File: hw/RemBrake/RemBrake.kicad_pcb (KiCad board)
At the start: 2 copper layers, 40 x 80 mm, 110 parts, among them IC1 LTC2943IDD#TRPBF, J1 Screw_Terminal_01x02, J2 Conn_01x03_MountingPin, J3 Screw_Terminal_01x04, J4 Conn_01x08_MountingPin, J5 Conn_01x04_MountingPin, J6 Conn_01x03_MountingPin, J7 Conn_01x07, J8 Conn_01x07, J9 Conn_01x03, Q1 SiS415DNT, Q2 BC337, Q3 BC847, Q4 BC337, Q5 BC847, Q6 BC337, Q7 BC847, Q8 BC337, Q9 BC847, U1 TPS62140, U2 BD48ExxG, U3 XC6220B331MR, U4 MAX40200AUK, U5 LM555xN, U6 MAX40200AUK, U7 MAX40200AUK

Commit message: added 555 counter output divider to adjust to 3v3 voltage level
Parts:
- added R46: 5k, Resistor_SMD:R_0805_2012Metric_Pad1.20x1.40mm_HandSolder, B.Cu at (127.6, 104.1)
- added R47: 5k, Resistor_SMD:R_0805_2012Metric_Pad1.20x1.40mm_HandSolder, B.Cu at (128.9, 106.6)
- added REF**: OSHW-Symbol_6.7x6mm_SilkScreen, Symbol:OSHW-Symbol_6.7x6mm_SilkScreen, B.Cu at (153.4, 66.6)
- added REF**: WEEE-Logo_4.2x6mm_SilkScreen, Symbol:WEEE-Logo_4.2x6mm_SilkScreen, B.Cu at (153.4, 74.1)
- renumbered R46 to R48, R47 to R49, R48 to R50, R49 to R51, R50 to R52, R51 to R53, R52 to R54, R53 to R55, R54 to R56, R55 to R57, R56 to R58, R57 to R59, R58 to R60, R59 to R61, R60 to R62, R61 to R63
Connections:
- U5 pad 3: Net-(D3-A) -> Net-(U5-Q)
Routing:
- added copper zone on B.Cu, net Net-(U5-Q)

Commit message: updated pcb and added todo in the schematic
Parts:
- added D3: MBR0520, Diode_SMD:D_SOD-123, F.Cu at (135.6, 123.7)
- added R46: 536k, Resistor_SMD:R_0805_2012Metric_Pad1.20x1.40mm_HandSolder, F.Cu at (131.9, 124.5)
- C5, C6: value 220nF -> 0.1uF
- R17, R3, R33, R39: value 5k -> 5k1
- R28, R29, R30: value 100R -> 110R
- R36: value 200R -> 110R
- R47: renamed from R46; value 5k -> 5k1
- R48: renamed from R47; value 5k -> 10k
- R49: renamed from R48; value 5k -> 2k7
- R55: renamed from R54; value 5k -> 5k1
- R59: renamed from R58; value 590k -> 10k
- R9: value 590k -> 536k
- moved C10 3.74 mm to (137.3, 129.1), turned to -90 degrees
- moved C7 3.11 mm to (132.2, 121.5), turned to 0 degrees
- moved R59 2.54 mm to (136.3, 126.0)
- moved C9 1.89 mm to (135.0, 129.1), turned to -90 degrees
- moved C8 0.54 mm to (132.7, 129.1), turned to -90 degrees
- moved R30 0.16 mm to (136.3, 121.5)
- renumbered D3 to D4, R49 to R50, R50 to R51, R51 to R52, R52 to R53, R53 to R54, R55 to R56, R56 to R57, R57 to R58, R59 to R60, R60 to R61, R61 to R62, R62 to R63, R63 to R64
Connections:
- C7 pad 1: /brake_control/STATUS -> Net-(D3-A)
- U5 pad 4: /brake_control/STATUS -> Net-(D3-A)
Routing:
- net Net-(D3-A): track 0.00 -> 23.5 mm
- net /brake_control/STATUS: track 67.3 -> 59.1 mm
- net /brake_control/ENABLE: track 55.3 -> 58.1 mm
- net /brake_control/BUZZER: track 33.1 -> 35.6 mm
- net +5V: track 76.8 -> 78.9 mm
- net /brake_control/I2C.SDA: track 92.9 -> 94.5 mm
- net +3V3: track 108.4 -> 107.0 mm
- net /brake_control/I2C.SCL: track 85.6 -> 87.0 mm
- net GND: vias 6 -> 7
- added copper zone on F.Cu, net Net-(D3-A)

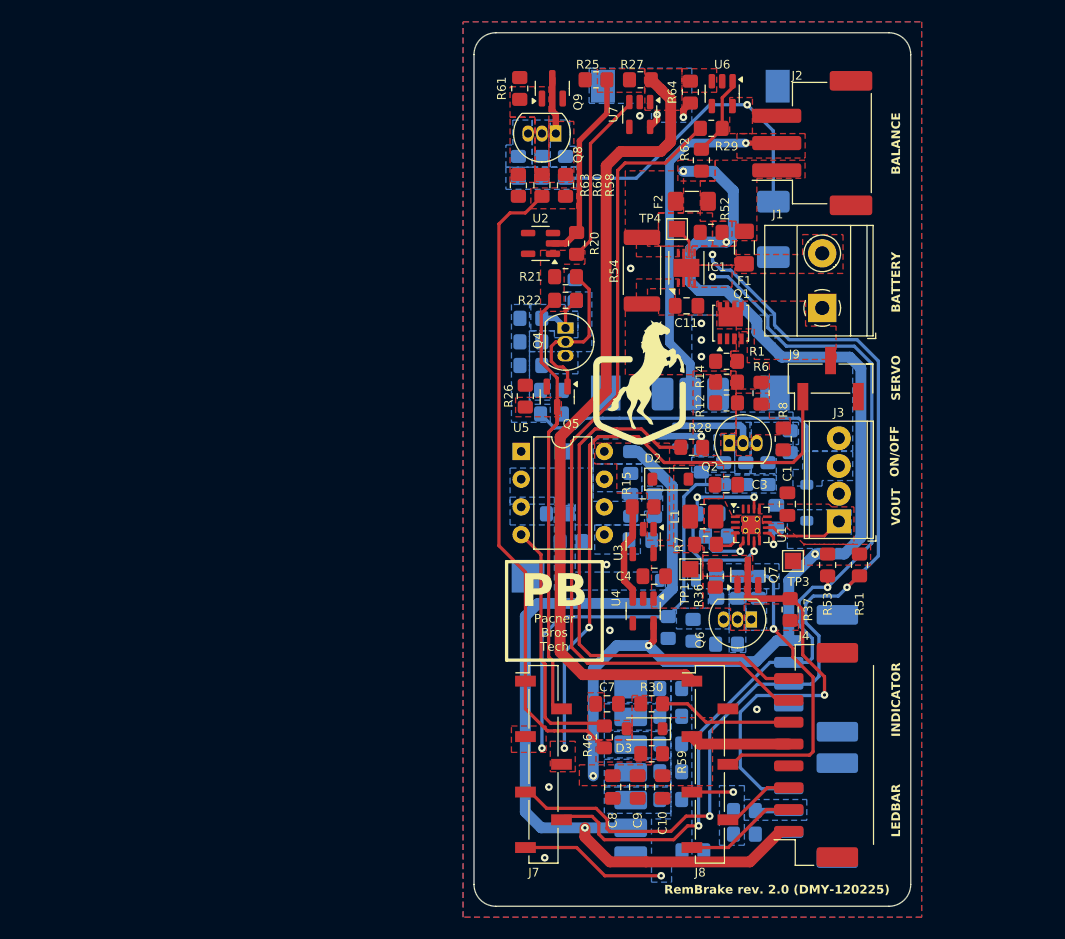
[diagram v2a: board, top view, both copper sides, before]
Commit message: replaced optocoupler with transistor and loaded components in the pcb sheet
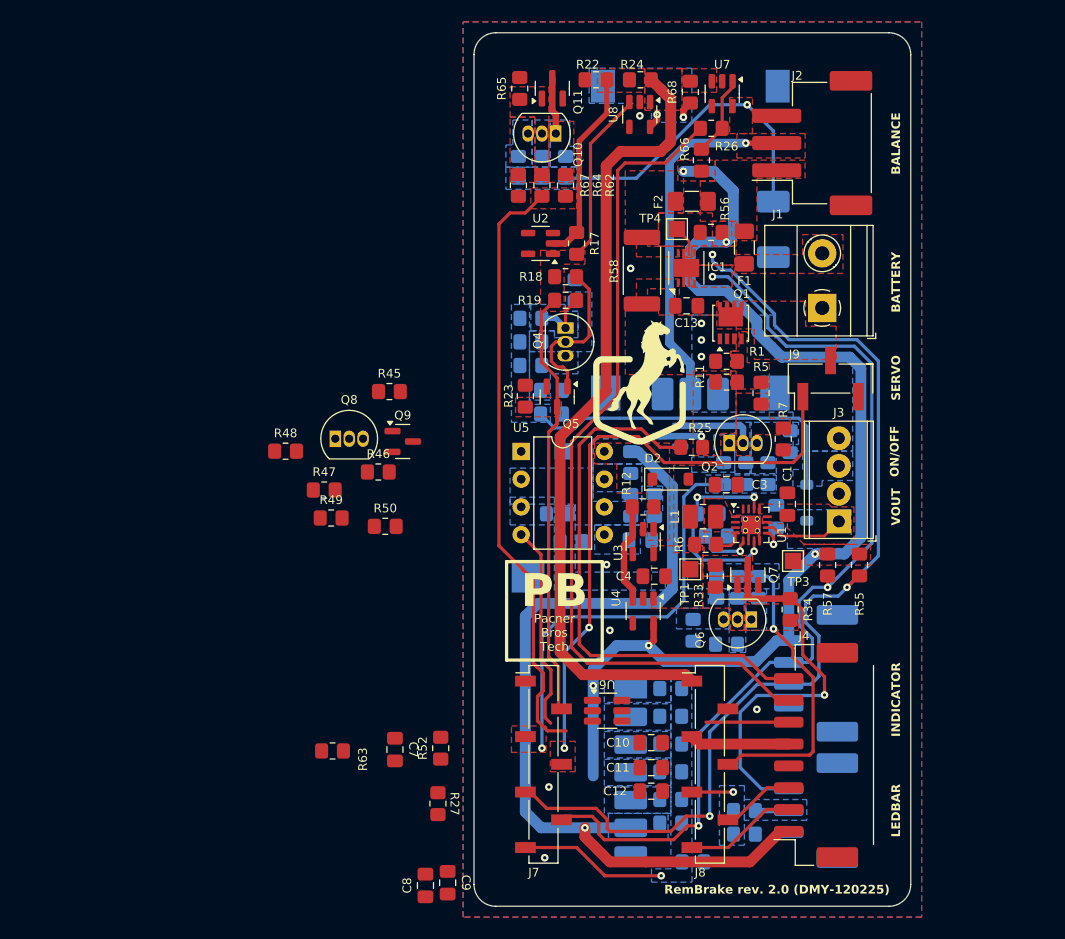
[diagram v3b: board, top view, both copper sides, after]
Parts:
- removed D3, D4: MBR0520, Diode_SMD:D_SOD-123
- removed the R11 at (140.8, 99.2)
- removed the R12 at (143.1, 93.9)
- removed the R2 at (137.8, 114.5)
- removed REF**: OSHW-Symbol_6.7x6mm_SilkScreen, Symbol:OSHW-Symbol_6.7x6mm_SilkScreen
- removed REF**: WEEE-Logo_4.2x6mm_SilkScreen, Symbol:WEEE-Logo_4.2x6mm_SilkScreen
- added C8: 0.33uF, Capacitor_SMD:C_0805_2012Metric_Pad1.18x1.45mm_HandSolder, F.Cu at (115.6, 138.1)
- added C9: 0.33uF, Capacitor_SMD:C_0805_2012Metric_Pad1.18x1.45mm_HandSolder, F.Cu at (117.6, 137.8)
- added Q8: BC337, Package_TO_SOT_THT:TO-92_Inline, F.Cu at (107.3, 97.2)
- added Q9: BC847, Package_TO_SOT_SMD:SOT-23, F.Cu at (113.5, 97.4)
- added R45: 100k, Resistor_SMD:R_0805_2012Metric_Pad1.20x1.40mm_HandSolder, F.Cu at (112.3, 92.9)
- added R47: 5k, Resistor_SMD:R_0805_2012Metric_Pad1.20x1.40mm_HandSolder, F.Cu at (106.3, 101.9)
- added R48: 5k, Resistor_SMD:R_0805_2012Metric_Pad1.20x1.40mm_HandSolder, F.Cu at (102.7, 98.3)
- added R49: 0R, Resistor_SMD:R_0805_2012Metric_Pad1.20x1.40mm_HandSolder, F.Cu at (106.9, 104.4)
- added R50: 0R, Resistor_SMD:R_0805_2012Metric_Pad1.20x1.40mm_HandSolder, F.Cu at (111.9, 105.2)
- added R51: 100k, Resistor_SMD:R_0805_2012Metric_Pad1.20x1.40mm_HandSolder, B.Cu at (138.0, 132.4)
- added R52: 5k1, Resistor_SMD:R_0805_2012Metric_Pad1.20x1.40mm_HandSolder, F.Cu at (117.0, 125.5)
- added U6: BD5230G-TR, Package_TO_SOT_SMD:SOT-23-6_Handsoldering, F.Cu at (132.2, 122.1)
- C7: value 47uF -> 680pF
- R46: value 536k -> 5k1
- moved R46 31.9 mm to (111.2, 100.2), turned to 0 degrees
- moved R63 29.2 mm to (107.0, 125.8)
- moved R27 21.6 mm to (116.7, 130.6), turned to -90 degrees
- moved C7 19.9 mm to (112.8, 125.6), turned to -90 degrees
- moved C10 5.39 mm to (136.2, 125.0), turned to 180 degrees
- moved C11 2.17 mm to (136.2, 127.3), turned to 180 degrees
- moved C12 1.11 mm to (136.2, 129.5), turned to 180 degrees
- moved R42 1.02 mm to (140.1, 135.9)
- renumbered C8 to C10, C9 to C11, C10 to C12, C11 to C13, Q8 to Q10, Q9 to Q11, R13 to R10, R14 to R11, R15 to R12, R16 to R13, R17 to R14, R18 to R15, R19 to R16, R20 to R17, R21 to R18, R22 to R19, R3 to R2, R23 to R20, R24 to R21, R25 to R22, R26 to R23, R27 to R24, R28 to R25, R29 to R26, R30 to R27, R31 to R28, R32 to R29, R4 to R3, R33 to R30, R34 to R31, R35 to R32, R36 to R33, R37 to R34, R38 to R35, R39 to R36, R40 to R37, R41 to R38, R42 to R39, R5 to R4, R43 to R40, R44 to R41, R45 to R42, R47 to R43, R48 to R44, R6 to R5, R49 to R53, R50 to R54, R51 to R55, R52 to R56, R53 to R57, R54 to R58, R55 to R59, R7 to R6, R56 to R60, R57 to R61, R58 to R62, R59 to R63, R60 to R64, R61 to R65, R62 to R66, R63 to R67, R64 to R68, R8 to R7, R9 to R8, R10 to R9, U6 to U7, U7 to U8
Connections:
- C7 pad 1: Net-(D3-A) -> /brake_control/STATUS
- J7 pad 1: /brake_control/STATUS -> /brake_control/READY
- J7 pad 3: /brake_control/POWER SW -> /brake_control/POWER
- Q3 pad 3: /control_connector/LED RED -> Net-(Q2-C)
- R11 pad 1: /control_connector/LED RED -> Net-(Q2-C)
- R2 pad 1: /brake_control/POWER SW -> /brake_control/POWER
- R25 pad 1: /control_connector/LED RED -> /brake_control/RUNNIG (RED)
- R3 pad 1: /brake_control/POWER SW -> /brake_control/POWER
- R4 pad 1: /brake_control/POWER SW -> /brake_control/POWER
- R43 pad 2: Net-(D4-A) -> /brake_control/BUZZ
- R44 pad 2: Net-(D4-A) -> /brake_control/BUZZ
- R46 pad 1: Net-(D3-A) -> /brake_control/POWER
- R46 pad 2: /brake_control/STATUS -> /brake_control/RUNNIG (RED)
- U5 pad 4: Net-(D3-A) -> /brake_control/BEEP
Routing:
- net /brake_control/POWER SW: track 37.7 -> 0.00 mm, vias 1 -> 0
- net /brake_control/POWER: track 0.00 -> 37.7 mm, vias 0 -> 1
- net Net-(D3-A): track 23.5 -> 0.00 mm
- net /brake_control/BEEP: track 0.00 -> 18.8 mm
- net /control_connector/LED RED: track 5.28 -> 0.00 mm, vias 1 -> 0
- net (no net): track 0.00 -> 5.28 mm
- net /control_connector/BLUE: track 12.4 -> 7.59 mm
- net /brake_control/STATUS: track 59.1 -> 55.9 mm
- net /brake_control/RUNNIG (RED): vias 0 -> 1
- added copper zone on B.Cu, net /brake_control/POWER
- added copper zone on F.Cu, net /brake_control/POWER
- added copper zone on F.Cu, net Net-(Q2-C)
- added copper zone on B.Cu, net Net-(Q8-B)
- added copper zone on F.Cu, net Net-(Q8-B)
- added copper zone on B.Cu, net Net-(Q8-E)
- added copper zone on F.Cu, net Net-(Q8-E)
- removed copper zone on B.Cu, net /brake_control/POWER SW
- removed copper zone on F.Cu, net /brake_control/POWER SW
- removed copper zone on F.Cu, net /control_connector/LED RED
- removed copper zone on F.Cu, net Net-(D3-A)
- removed copper zone on B.Cu, net Net-(D4-A)
- removed copper zone on B.Cu, net Net-(Q10-B)
- removed copper zone on F.Cu, net Net-(Q10-B)
- removed copper zone on B.Cu, net Net-(Q10-E)
- removed copper zone on F.Cu, net Net-(Q10-E)

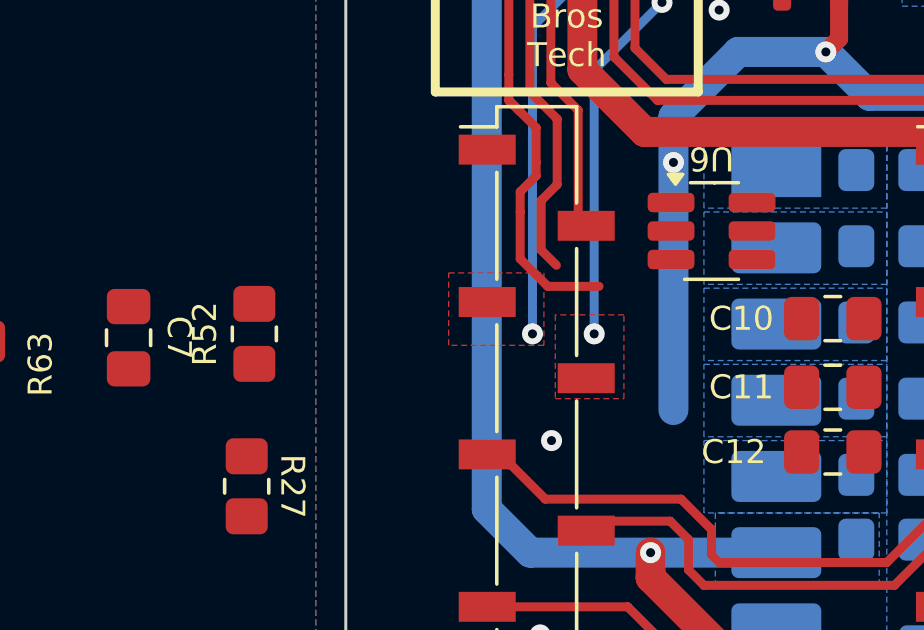
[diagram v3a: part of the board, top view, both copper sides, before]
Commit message: version update and added missing connection between VBUS and 5V
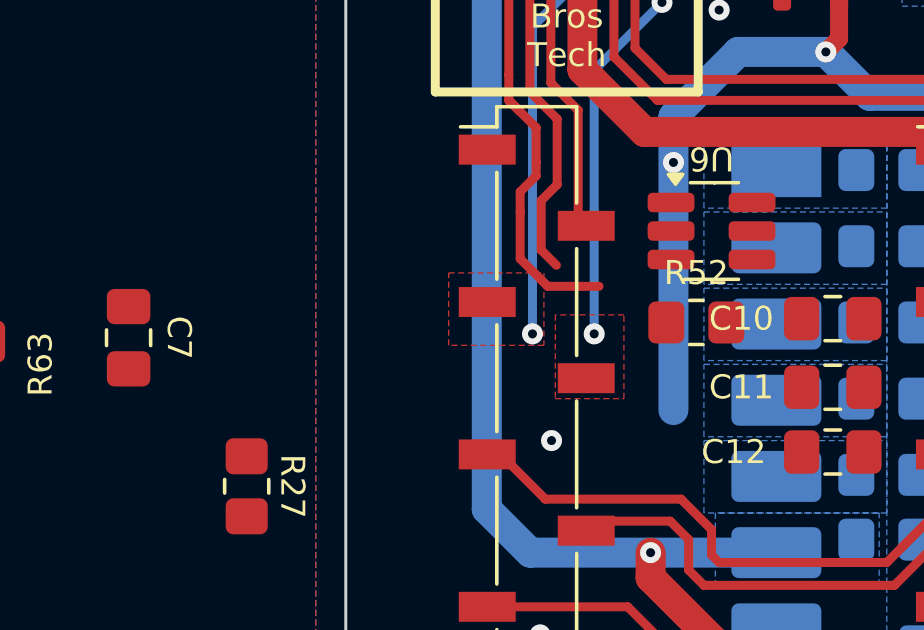
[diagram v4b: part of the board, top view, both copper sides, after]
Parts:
- moved R52 14.7 mm to (131.7, 125.1), turned to 0 degrees

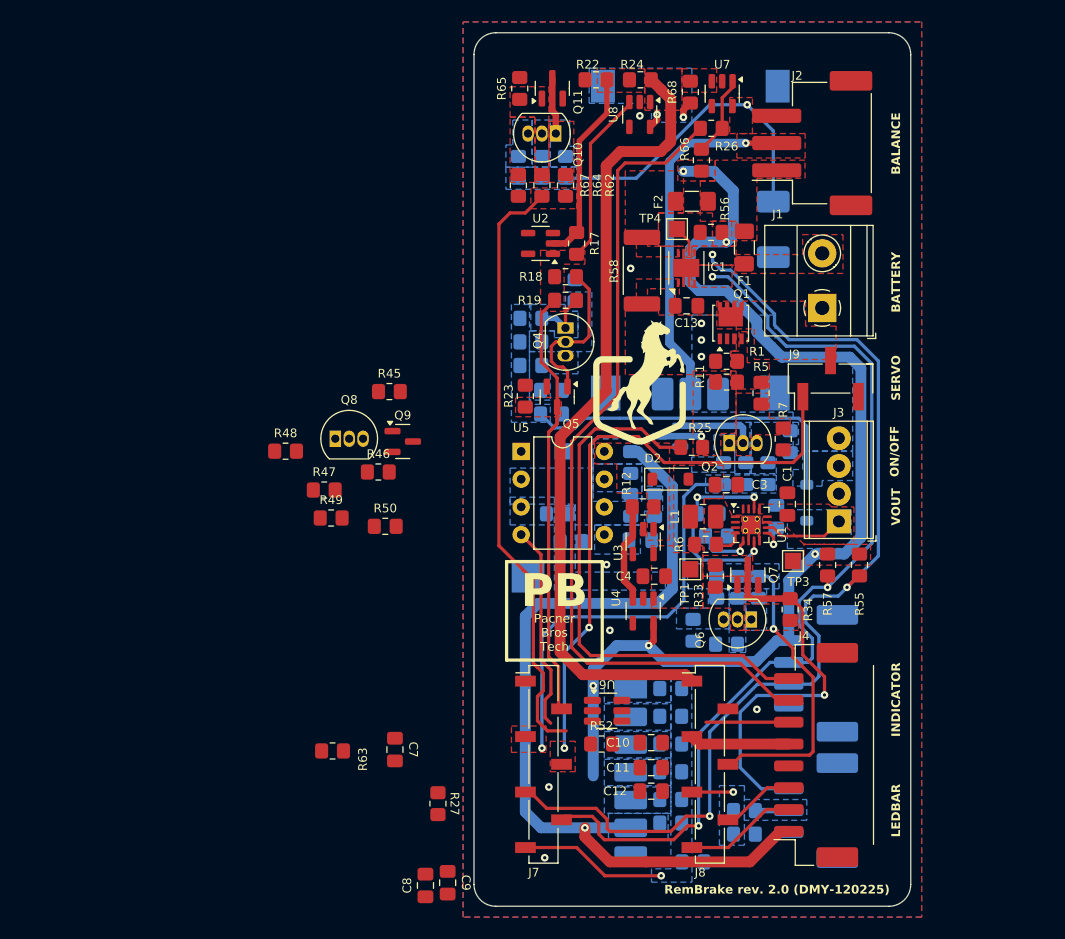
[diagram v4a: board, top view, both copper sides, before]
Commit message: added diodes to connect voltages to display and remote button even when connected to charger
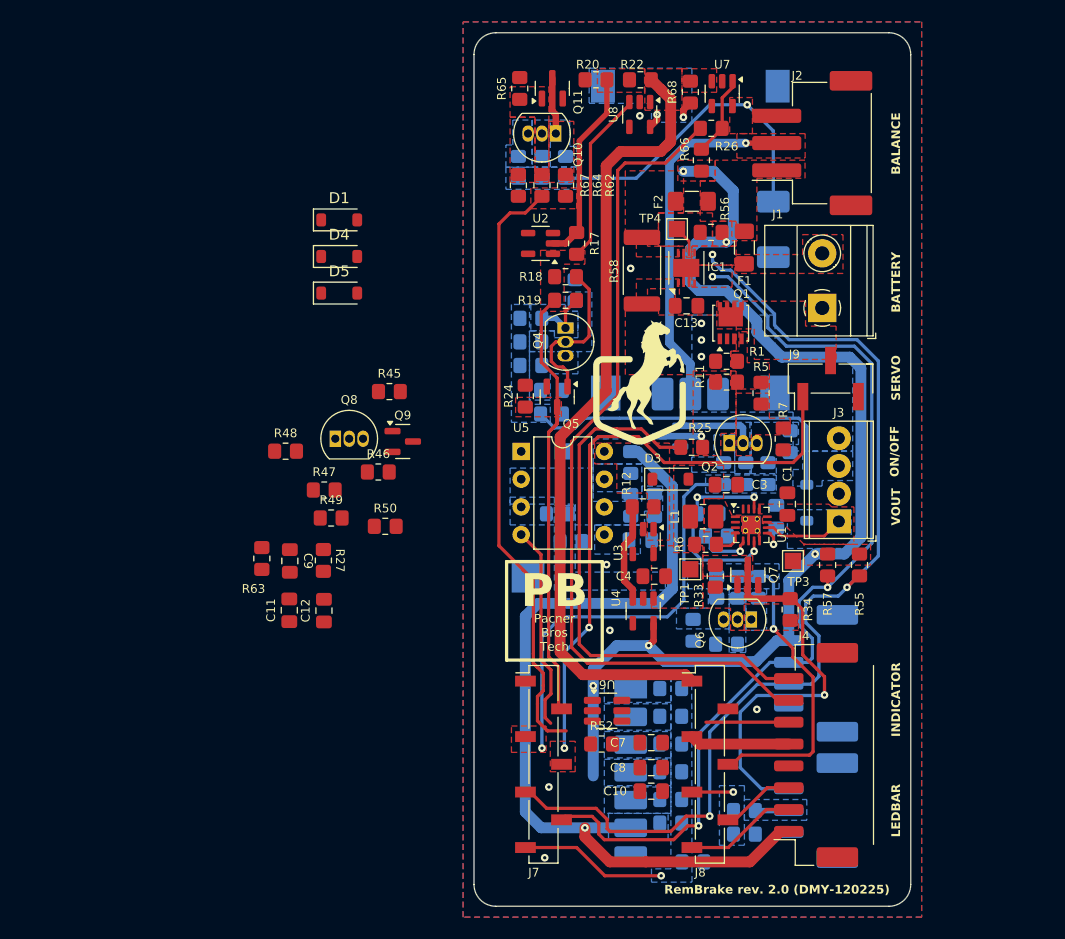
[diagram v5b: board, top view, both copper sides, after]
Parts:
- added D1: MBR0520, Diode_SMD:D_SOD-123, F.Cu at (107.7, 77.1)
- added D4: MBR0520, Diode_SMD:D_SOD-123, F.Cu at (107.7, 80.5)
- added D5: MBR0520, Diode_SMD:D_SOD-123, F.Cu at (107.7, 83.8)
- moved C11 28.1 mm to (103.1, 112.9)
- moved C12 27.4 mm to (106.3, 112.9), turned to 90 degrees
- moved R27 24.6 mm to (106.2, 108.3)
- moved C9 19.8 mm to (103.1, 108.4)
- moved R63 18.8 mm to (100.6, 108.1), turned to 90 degrees
- renumbered C12 to C10, C8 to C11, C9 to C12, C10 to C7, C11 to C8, C7 to C9, D1 to D2, D2 to D3, R22 to R20, R20 to R21, R24 to R22, R21 to R23, R23 to R24
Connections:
- C1 pad 1: /power_switch/BOOST -> Net-(D2-K)
- C3 pad 1: Net-(D2-A) -> +5V
- D2 pad 1: /power_switch/BOOST -> Net-(D2-K)
- D3 pad 1: +5V -> VDD
- D3 pad 2: Net-(D2-A) -> +5V
- J4 pad 1: +5V -> VDD
- L1 pad 2: Net-(D2-A) -> +5V
- M1 pad 6: +5V -> VDD
- R6 pad 1: Net-(D2-A) -> +5V
- R8 pad 1: Net-(D2-A) -> +5V
- U1 pad 10: /power_switch/BOOST -> Net-(D2-K)
- U1 pad 11: /power_switch/BOOST -> Net-(D2-K)
- U1 pad 12: /power_switch/BOOST -> Net-(D2-K)
- U1 pad 13: /power_switch/BOOST -> /power_switch/ON/OFF
- U1 pad 14: Net-(D2-A) -> +5V
- U1 pad 7: Net-(D2-A) -> +5V
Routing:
- net Net-(D2-A): track 23.9 -> 0.00 mm, vias 3 -> 0
- net +5V: track 78.9 -> 102.8 mm, vias 1 -> 4
- removed copper zone on F.Cu, net Net-(D2-A)

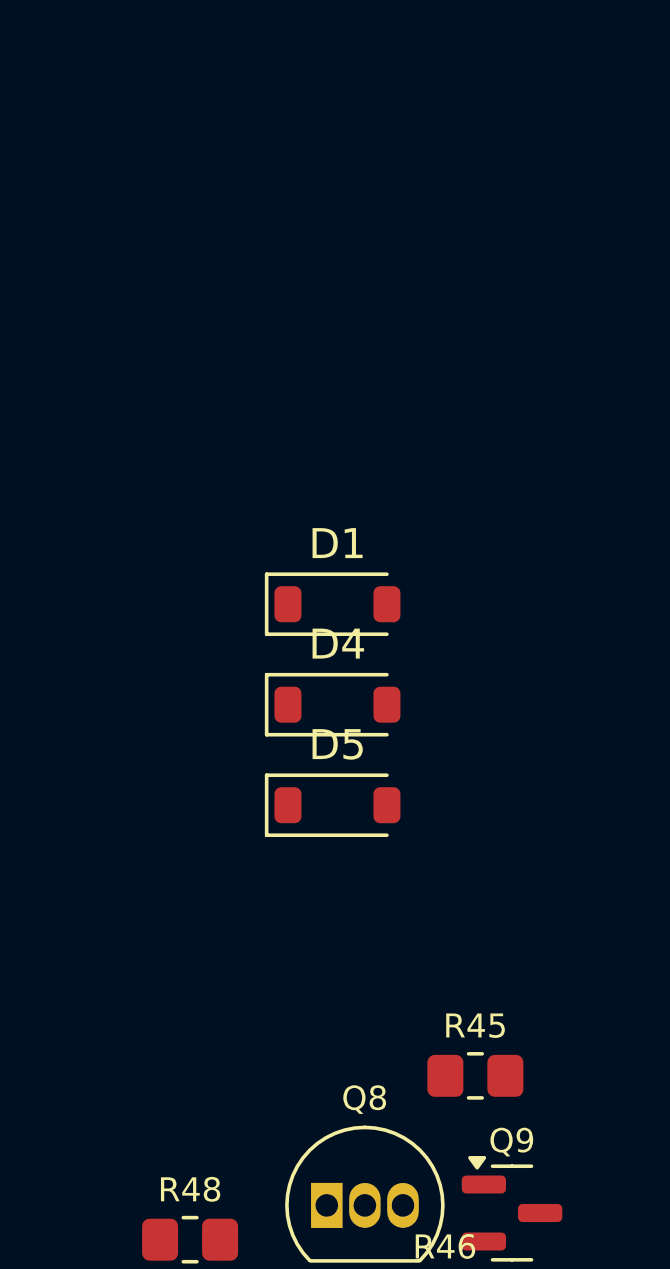
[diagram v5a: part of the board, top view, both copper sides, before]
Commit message: adjusted connections to be able to use bc337
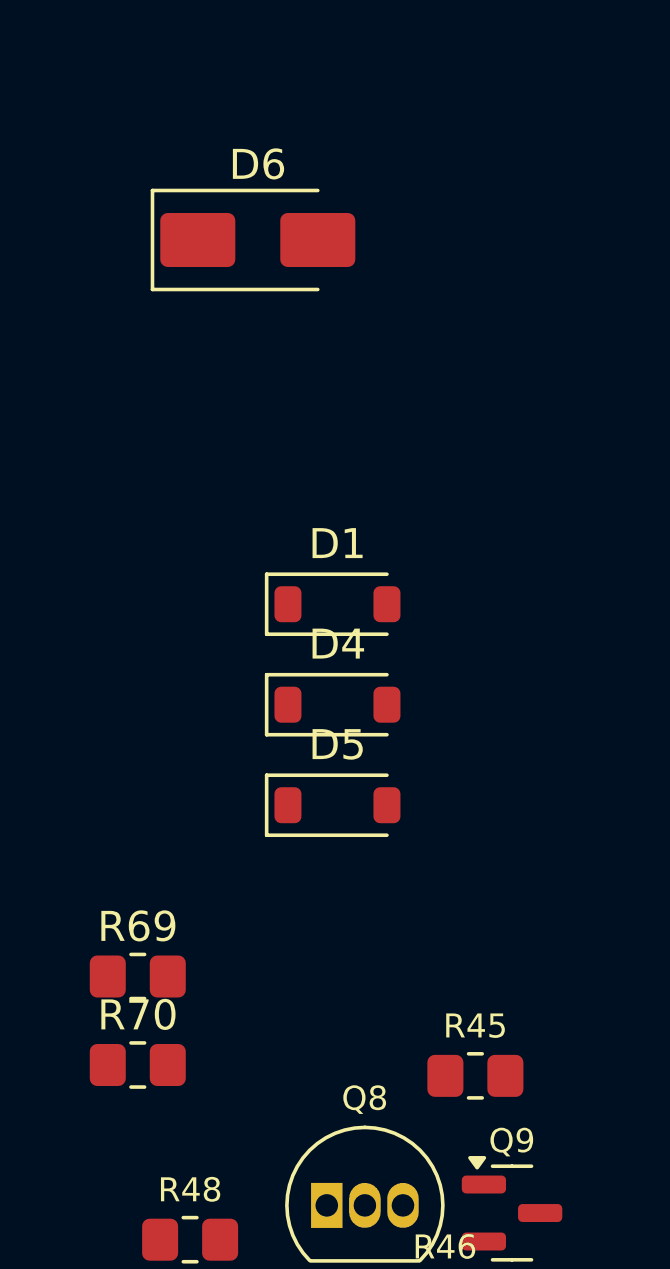
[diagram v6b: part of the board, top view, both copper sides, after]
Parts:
- added D6: SS1200, Diode_SMD:D_SMA, F.Cu at (105.0, 65.0)
- added R69: 0R, Resistor_SMD:R_0805_2012Metric_Pad1.20x1.40mm_HandSolder, F.Cu at (101.0, 89.5)
- added R70: 0R, Resistor_SMD:R_0805_2012Metric_Pad1.20x1.40mm_HandSolder, F.Cu at (101.0, 92.5)
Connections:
- Q8 pad 1: /brake_control/RUNNIG (RED) -> Net-(Q8-C)
- Q9 pad 3: /brake_control/RUNNIG (RED) -> Net-(Q8-C)
- R46 pad 2: /brake_control/RUNNIG (RED) -> Net-(Q8-C)
